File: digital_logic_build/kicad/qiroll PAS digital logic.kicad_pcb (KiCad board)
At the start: 2 copper layers, 49.5 x 32.4 mm, 47 parts, among them J1 brk_sense, J2 led_sw1, J4 mode_thr_batt, J5 pas_sense, U1 4093B, U2 4027B, U3 4093B, U5 4093B, U6 14538B, U7 L78L05_TO92

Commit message: version 2.5
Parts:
- removed J1: brk_sense, Connector_PinHeader_2.54mm:PinHeader_1x02_P2.54mm_Vertical
- added J3: accessory, Connector_PinHeader_2.54mm:PinHeader_1x03_P2.54mm_Vertical, F.Cu at (145.5, 103.8)
- D2, D3, D4, D5: value D_Schottky_Small -> D
- J2: footprint Connector_PinHeader_2.54mm:PinHeader_1x03_P2.54mm_Vertical -> Connector_PinHeader_2.54mm:PinHeader_1x04_P2.54mm_Vertical
- J5: value pas_sense -> 3_pin
- R2: value 1.6k -> 75k
- R7: value 1.6k -> 3.3k
- U7: value L78L05_TO92 -> MCP1799_3V3; footprint Package_TO_SOT_THT:TO-92_Inline -> Package_TO_SOT_SMD:SOT-23
- moved D2 12.6 mm to (128.9, 106.9), turned to 180 degrees
- moved J4 9.85 mm to (117.8, 103.8), turned to 90 degrees
- moved R7 4.63 mm to (114.7, 110.3), turned to 90 degrees
- moved J5 2.62 mm to (149.3, 103.8), turned to 90 degrees
- moved D3 2.37 mm to (125.7, 107.5), turned to 90 degrees
- moved F1 2.11 mm to (118.3, 106.9), turned to 0 degrees
- moved U7 1.54 mm to (122.9, 108.0), turned to 180 degrees
- moved D1 0.92 mm to (118.3, 110.3)
- moved J2 0.50 mm to (136.8, 103.8)
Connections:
- J2 pad 2: Net-(C2-Pad2) -> Net-(D2-Pad1)
- J2 pad 3: Net-(J2-Pad3) -> Net-(C2-Pad2)
- J5 pad 1: VDD -> Net-(D2-Pad1)
- J5 pad 3: Net-(J5-Pad3) -> Net-(F1-Pad2)
- R5 pad 2: Net-(J5-Pad3) -> Net-(J3-Pad3)
- U3 pad 3: Net-(J2-Pad3) -> Net-(J2-Pad4)
- U6 pad 4: Net-(J5-Pad3) -> Net-(J3-Pad3)
- U7 pad 1: VDD -> GND
- U7 pad 2: GND -> VDD
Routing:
- net Net-(F1-Pad2): track 10.4 -> 43.1 mm
- net VDD: track 200.6 -> 176.0 mm, vias 4 -> 5
- net Net-(J3-Pad3): track 0.00 -> 23.6 mm
- net Net-(J5-Pad3): track 22.3 -> 0.00 mm
- net Net-(J2-Pad4): track 0.00 -> 15.6 mm
- net Net-(J2-Pad3): track 12.8 -> 0.00 mm
- net GND: track 71.7 -> 64.4 mm, vias 15 -> 25
- net Net-(D2-Pad1): track 68.6 -> 62.3 mm, vias 2 -> 3
- net Net-(D2-Pad2): track 11.8 -> 5.59 mm, vias 1 -> 0
- net Net-(C10-Pad1): track 22.3 -> 18.0 mm, vias 1 -> 0
- net Net-(D3-Pad1): track 9.35 -> 12.9 mm
- net Net-(C2-Pad2): track 26.1 -> 29.1 mm
- net Net-(F1-Pad1): track 1.89 -> 3.43 mm
- net Net-(J4-Pad3): track 22.6 -> 23.4 mm
- added copper zone on F.Cu, net GND
- added copper zone on F.Cu, net VDD
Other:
- board text added: "3.3v"
- board text added: "J3"
- board text added: "qiroll pedal assist v2.5 Eric Dasmalchi"
- board text added: "std kit: don’t install D2"
- board text removed: "+5v"
- board text removed: "J1"
- board text removed: "qiroll pedal assist v2.3 Eric Dasmalchi"

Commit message: clarify silkscreen
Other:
- board text added: "D2 Pro kit only"
- board text added: "D5 Pro kit only"
- board text removed: "std kit: don’t install D2"

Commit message: even tidier schematic
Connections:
- U5 pad 8: Net-(U2-Pad12) -> Net-(U1-Pad9)
- U5 pad 9: Net-(U1-Pad9) -> Net-(U2-Pad12)
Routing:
- net Net-(U1-Pad9): track 36.1 -> 32.8 mm

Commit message: add simple, update main pcb to KiCad 6
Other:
- net class Default removed

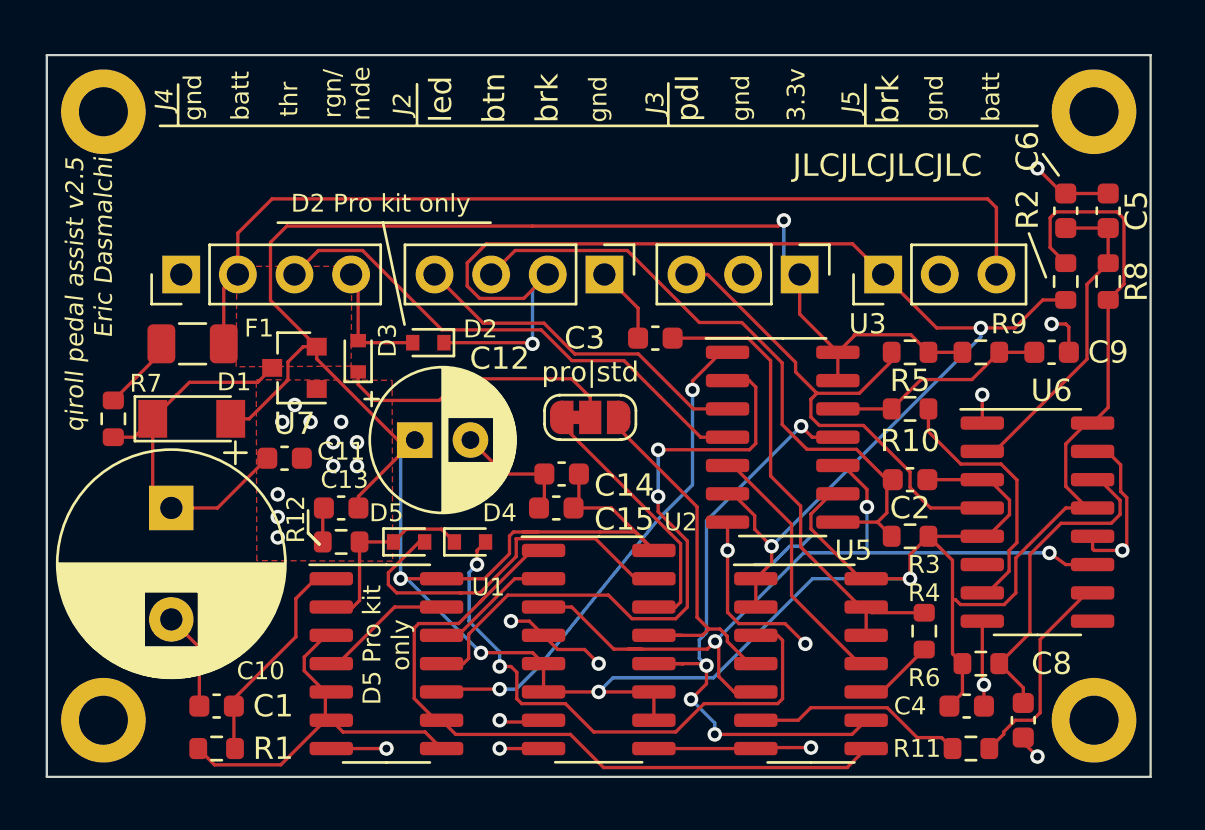
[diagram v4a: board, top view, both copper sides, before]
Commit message: update pcb to new kicad
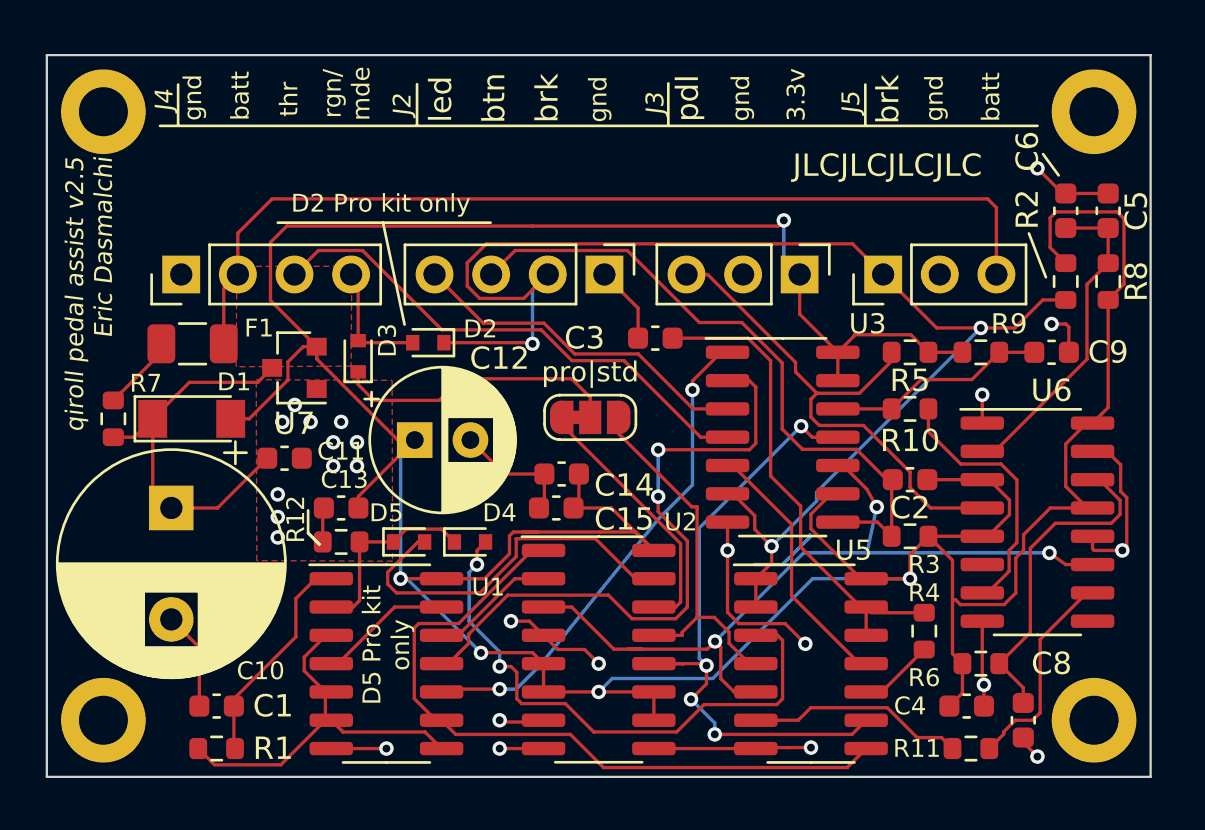
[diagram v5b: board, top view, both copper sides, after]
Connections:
- U6 pad 6: Net-(U6-Pad6) -> unconnected-(U6A-Q-Pad6)
- U6 pad 9: Net-(U6-Pad9) -> unconnected-(U6B-~{Q}-Pad9)
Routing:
- net Net-(J2-Pin_3): track 29.1 -> 29.7 mm
- net Net-(JP1-B): track 17.3 -> 16.7 mm

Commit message: revise footprints
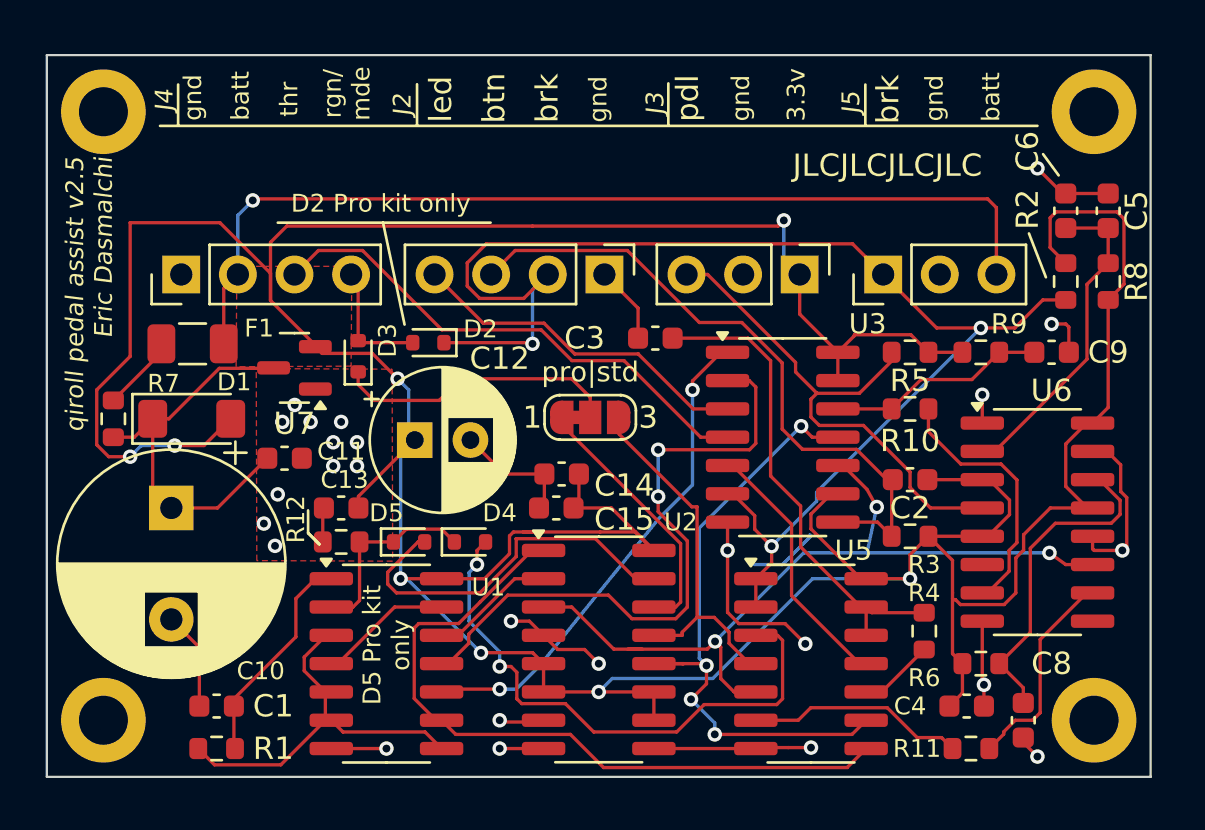
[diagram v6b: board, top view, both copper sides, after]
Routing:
- net VDD: track 176.4 -> 198.2 mm, vias 5 -> 8
- net Net-(J4-Pin_2): track 43.1 -> 43.5 mm, vias 0 -> 1

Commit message: bigger silkscreen
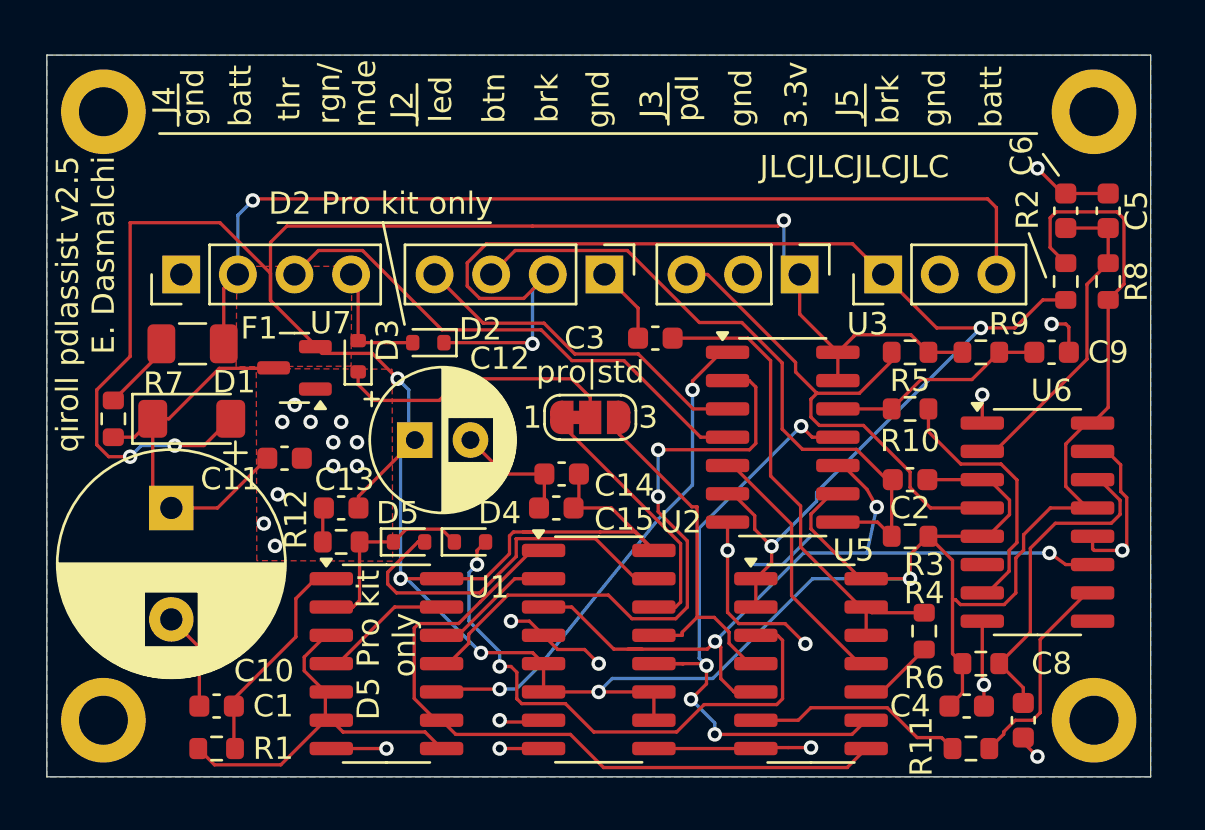
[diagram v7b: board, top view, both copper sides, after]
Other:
- board text added: "qiroll pdlassist v2.5 E. Dasmalchi"
- board text removed: "qiroll pedal assist v2.5 Eric Dasmalchi"
